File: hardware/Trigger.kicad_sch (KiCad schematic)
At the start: 2 parts, among them U6 MCP47FEB02A0T-E/ST, U7 Opamp_Dual

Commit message: Trig
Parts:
- added C30: 100n, symbol Device:C
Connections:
- net GND: now reaches U7.4 (V-)
- net GND: now also U6.5 (VSS), U6.6 (LAT/HVC), C30.1
- net VSYS: now reaches U7.8 (V+)
- net VSYS: now also U6.1 (VDD)
- net TRIG: now reaches U7.1
- net TRIG: now also U7.7
- net at U7.2 (-): now also U6.4 (VOUT1)
- net ASIG: now reaches U7.3 (+)
- net VREF: now reaches U6.2 (VREF)
- net VREF: now also C30.2
- net at U6.3 (VOUT0): now also U7.6 (-)
- net SDA: now reaches U6.7 (SCL)
- net SCL: now reaches U6.8 (SDA)
- net ASIG2: now reaches U7.5 (+)
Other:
- note added: "Possible resistor at TRIG output?"
- moved on the sheet: U6, U7C

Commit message: Trig finished
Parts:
- added C28: C, symbol Device:C
- added R14, R15: 0, symbol Device:R
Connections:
- net ASIG: now also R14.1; no longer U7.3 (+)
- net ASIG2: now also R15.2; no longer U7.5 (+)
- net GND: now also C28.2
- net TRIG: no longer U7.7
- net VSYS: now also C28.1
- new net: R15.1, U7.5 (+)
- new net: R14.2, U7.3 (+)
- new net TRIG2: U7.7

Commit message: updated trig
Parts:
- removed R14, R15: 0, symbol Device:R
- C28: value C -> 100n
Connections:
- net ASIG: now also U7.3 (+)
- net ASIG2: now also U7.5 (+)
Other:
- note removed: "Possible resistor at TRIG output?"
- moved on the sheet: C28, U7C
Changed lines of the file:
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@@
 	(generator_version "9.0")
 	(paper "A4")
-	(text "Possible resistor at TRIG output?\n"
-		(exclude_from_sim no)
-		(at 182.626 53.848 0)
-		(effects
-			(font
-				(size 1.27 1.27)
-			)
-		)
-	)
 	(junction
-		(at 184.15 69.85)
+		(at 187.96 74.93)
 		(diameter 0)
 		(color 0 0 0 0)
@@
 	(wire
 		(pts
-			(xy 143.51 62.23) (xy 151.13 62.23)
-		)
-		(stroke
-			(width 0)
-			(type default)
-		)
-	)
-	(wire
-		(pts
 			(xy 134.62 104.14) (xy 134.62 88.9)
 		)
@@
 	(wire
 		(pts
-			(xy 184.15 66.04) (xy 184.15 69.85)
+			(xy 191.77 74.93) (xy 187.96 74.93)
 		)
 		(stroke
@@
 	(wire
 		(pts
-			(xy 184.15 86.36) (xy 184.15 87.63)
+			(xy 171.45 74.93) (xy 170.18 74.93)
 		)
 		(stroke
@@
 	(wire
 		(pts
-			(xy 143.51 44.45) (xy 151.13 44.45)
-		)
-		(stroke
-			(width 0)
-			(type default)
-		)
-	)
-	(wire
-		(pts
 			(xy 190.5 110.49) (xy 190.5 114.3)
 		)
@@
 	(wire
 		(pts
-			(xy 195.58 69.85) (xy 199.39 69.85)
-		)
-		(stroke
-			(width 0)
-			(type default)
-		)
-	)
-	(wire
-		(pts
-			(xy 125.73 44.45) (xy 135.89 44.45)
+			(xy 187.96 86.36) (xy 187.96 90.17)
+		)
+		(stroke
+			(width 0)
+			(type default)
+		)
+	)
+	(wire
+		(pts
+			(xy 125.73 44.45) (xy 151.13 44.45)
 		)
 		(stroke
@@
 	(wire
 		(pts
-			(xy 184.15 69.85) (xy 187.96 69.85)
+			(xy 187.96 74.93) (xy 187.96 78.74)
 		)
 		(stroke
@@
 	(wire
 		(pts
-			(xy 125.73 62.23) (xy 135.89 62.23)
-		)
-		(stroke
-			(width 0)
-			(type default)
-		)
-	)
-	(wire
-		(pts
-			(xy 184.15 69.85) (xy 184.15 71.12)
+			(xy 125.73 62.23) (xy 151.13 62.23)
+		)
+		(stroke
+			(width 0)
+			(type default)
+		)
+	)
+	(wire
+		(pts
+			(xy 187.96 74.93) (xy 186.69 74.93)
 		)
 		(stroke
@@
 	(hierarchical_label "VSYS"
 		(shape input)
-		(at 184.15 66.04 90)
+		(at 191.77 74.93 0)
 		(effects
 			(font
@@
 	(symbol
 		(lib_id "Device:Opamp_Dual")
-		(at 186.69 78.74 0)
+		(at 179.07 77.47 270)
 		(unit 3)
 		(exclude_from_sim no)
@@
 		(fields_autoplaced yes)
 		(property "Reference" "U7"
-			(at 185.42 77.4699 0)
+			(at 180.3401 76.2 0)
 			(effects
 				(font
@@
 		)
 		(property "Value" "Opamp_Dual"
-			(at 185.42 80.0099 0)
+			(at 177.8001 76.2 0)
 			(effects
 				(font
@@
 		)
 		(property "Footprint" "Package_DIP:DIP-8_W7.62mm_Socket_LongPads"
-			(at 186.69 78.74 0)
+			(at 179.07 77.47 0)
 			(effects
 				(font
@@
 		)
 		(property "Datasheet" "~"
-			(at 186.69 78.74 0)
+			(at 179.07 77.47 0)
 			(effects
 				(font
@@
 		)
 		(property "Description" "Dual operational amplifier"
-			(at 186.69 78.74 0)
+			(at 179.07 77.47 0)
 			(effects
 				(font
@@
 		)
 		(property "Sim.Library" "${KICAD9_SYMBOL_DIR}/Simulation_SPICE.sp"
-			(at 186.69 78.74 0)
+			(at 179.07 77.47 0)
 			(effects
 				(font
@@
 		)
 		(property "Sim.Name" "kicad_builtin_opamp_dual"
-			(at 186.69 78.74 0)
+			(at 179.07 77.47 0)
 			(effects
 				(font
@@
 		)
 		(property "Sim.Device" "SUBCKT"
-			(at 186.69 78.74 0)
+			(at 179.07 77.47 0)
 			(effects
 				(font
@@
 		)
 		(property "Sim.Pins" "1=out1 2=in1- 3=in1+ 4=vee 5=in2+ 6=in2- 7=out2 8=vcc"
-			(at 186.69 78.74 0)
+			(at 179.07 77.47 0)
 			(effects
 				(font
@@
 	)
 	(symbol
-		(lib_id "Device:R")
-		(at 139.7 62.23 270)
-		(unit 1)
-		(exclude_from_sim no)
-		(in_bom yes)
-		(on_board yes)
-		(dnp no)
-		(fields_autoplaced yes)
-		(property "Reference" "R15"
-			(at 139.7 55.88 90)
-			(effects
-				(font
-					(size 1.27 1.27)
-				)
-			)
-		)
-		(property "Value" "0"
-			(at 139.7 58.42 90)
-			(effects
-				(font
-					(size 1.27 1.27)
-				)
-			)
-		)
-		(property "Footprint" ""
-			(at 139.7 60.452 90)
-			(effects
-				(font
-					(size 1.27 1.27)
-				)
-				(hide yes)
-			)
-		)
-		(property "Datasheet" "~"
-			(at 139.7 62.23 0)
-			(effects
-				(font
-					(size 1.27 1.27)
-				)
-				(hide yes)
-			)
-		)
-		(property "Description" "Resistor"
-			(at 139.7 62.23 0)
-			(effects
-				(font
-					(size 1.27 1.27)
-				)
-				(hide yes)
-			)
-		)
-		(pin "2"
-		)
-		(pin "1"
-		)
-		(instances
-			(project ""
-				(path "/94683f5c-9cd9-448e-be96-9792537b5cb8/865345ee-93ca-410b-9293-676d9f6f2ef0"
-					(reference "R15")
-					(unit 1)
-				)
-			)
-		)
-	)
-	(symbol
 		(lib_id "Device:Opamp_Dual")
 		(at 158.75 46.99 0)
@@
 	(symbol
 		(lib_id "Device:C")
-		(at 191.77 69.85 90)
+		(at 187.96 82.55 0)
 		(unit 1)
 		(exclude_from_sim no)
@@
 		(fields_autoplaced yes)
 		(property "Reference" "C28"
-			(at 191.77 62.23 90)
-			(effects
-				(font
-					(size 1.27 1.27)
-				)
-			)
-		)
-		(property "Value" "C"
-			(at 191.77 64.77 90)
+			(at 195.58 82.55 90)
+			(effects
+				(font
+					(size 1.27 1.27)
+				)
+			)
+		)
+		(property "Value" "100n"
+			(at 193.04 82.55 90)
 			(effects
 				(font
@@
 		)
 		(property "Footprint" ""
-			(at 195.58 68.8848 0)
+			(at 188.9252 86.36 0)
 			(effects
 				(font
@@
 		)
 		(property "Datasheet" "~"
-			(at 191.77 69.85 0)
+			(at 187.96 82.55 0)
 			(effects
 				(font
@@
 		)
 		(property "Description" "Unpolarized capacitor"
-			(at 191.77 69.85 0)
+			(at 187.96 82.55 0)
 			(effects
 				(font
@@
 	(symbol
 		(lib_id "power:GND")
-		(at 184.15 87.63 0)
+		(at 170.18 74.93 270)
 		(unit 1)
 		(exclude_from_sim no)
@@
 		(fields_autoplaced yes)
 		(property "Reference" "#PWR030"
-			(at 184.15 93.98 0)
+			(at 163.83 74.93 0)
 			(effects
 				(font
@@
 		)
 		(property "Value" "GND"
-			(at 184.15 92.71 0)
+			(at 165.1 74.93 0)
 			(effects
 				(font
@@
 		)
 		(property "Footprint" ""
-			(at 184.15 87.63 0)
+			(at 170.18 74.93 0)
 			(effects
 				(font
@@
 		)
 		(property "Datasheet" ""
-			(at 184.15 87.63 0)
+			(at 170.18 74.93 0)
 			(effects
 				(font
@@
 		)
 		(property "Description" "Power symbol creates a global label with name \"GND\" , ground"
-			(at 184.15 87.63 0)
+			(at 170.18 74.93 0)
 			(effects
 				(font
@@
 				(path "/94683f5c-9cd9-448e-be96-9792537b5cb8/865345ee-93ca-410b-9293-676d9f6f2ef0"
 					(reference "#PWR030")
-					(unit 1)
-				)
-			)
-		)
-	)
-	(symbol
-		(lib_id "Device:R")
-		(at 139.7 44.45 90)
-		(unit 1)
-		(exclude_from_sim no)
-		(in_bom yes)
-		(on_board yes)
-		(dnp no)
-		(fields_autoplaced yes)
-		(property "Reference" "R14"
-			(at 139.7 38.1 90)
-			(effects
-				(font
-					(size 1.27 1.27)
-				)
-			)
-		)
-		(property "Value" "0"
-			(at 139.7 40.64 90)
-			(effects
-				(font
-					(size 1.27 1.27)
-				)
-			)
-		)
-		(property "Footprint" ""
-			(at 139.7 46.228 90)
-			(effects
-				(font
-					(size 1.27 1.27)
-				)
-				(hide yes)
-			)
-		)
-		(property "Datasheet" "~"
-			(at 139.7 44.45 0)
-			(effects
-				(font
-					(size 1.27 1.27)
-				)
-				(hide yes)
-			)
-		)
-		(property "Description" "Resistor"
-			(at 139.7 44.45 0)
-			(effects
-				(font
-					(size 1.27 1.27)
-				)
-				(hide yes)
-			)
-		)
-		(pin "2"
-		)
-		(pin "1"
-		)
-		(instances
-			(project ""
-				(path "/94683f5c-9cd9-448e-be96-9792537b5cb8/865345ee-93ca-410b-9293-676d9f6f2ef0"
-					(reference "R14")
 					(unit 1)
 				)
@@
 	(symbol
 		(lib_id "power:GND")
-		(at 199.39 69.85 90)
+		(at 187.96 90.17 0)
 		(unit 1)
 		(exclude_from_sim no)
@@
 		(fields_autoplaced yes)
 		(property "Reference" "#PWR039"
-			(at 205.74 69.85 0)
+			(at 187.96 96.52 0)
 			(effects
 				(font
@@
 		)
 		(property "Value" "GND"
-			(at 203.2 69.8499 90)
+			(at 187.9601 93.98 90)
 			(effects
 				(font
@@
 		)
 		(property "Footprint" ""
-			(at 199.39 69.85 0)
+			(at 187.96 90.17 0)
 			(effects
 				(font
@@
 		)
 		(property "Datasheet" ""
-			(at 199.39 69.85 0)
+			(at 187.96 90.17 0)
 			(effects
 				(font
@@
 		)
 		(property "Description" "Power symbol creates a global label with name \"GND\" , ground"
-			(at 199.39 69.85 0)
-			(effects
-				(font
+			(at 187.96 90.17 0)
+			(effects
+				(font

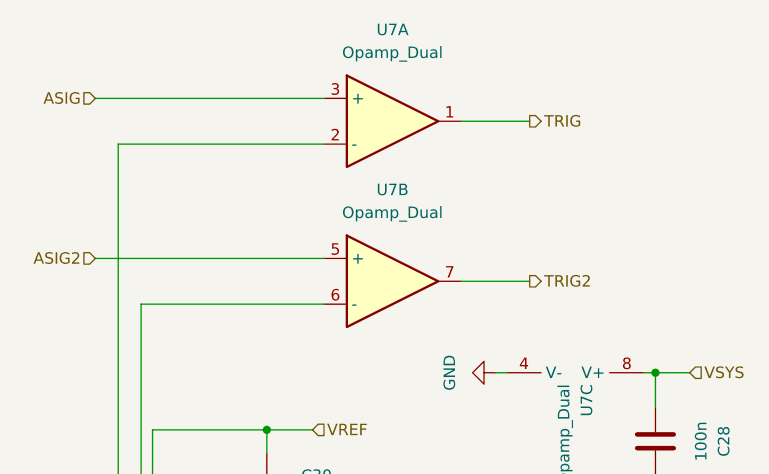
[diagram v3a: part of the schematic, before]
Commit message: connected analog i/o on main schematic and updated PSU naming
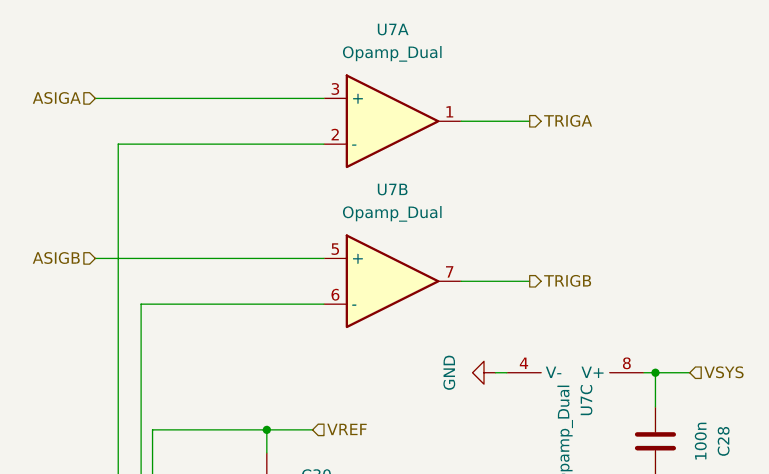
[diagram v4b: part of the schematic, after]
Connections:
- net ASIG renamed ASIGA
- net ASIG2 renamed ASIGB
- net TRIG renamed TRIGA
- net TRIG2 renamed TRIGB
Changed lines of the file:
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@@
 		)
 	)
-	(hierarchical_label "TRIG"
+	(hierarchical_label "TRIGA"
 		(shape output)
 		(at 173.99 46.99 0)
@@
 		)
 	)
-	(hierarchical_label "TRIG2"
+	(hierarchical_label "TRIGB"
 		(shape output)
 		(at 173.99 64.77 0)
@@
 		)
 	)
-	(hierarchical_label "ASIG"
+	(hierarchical_label "ASIGA"
 		(shape input)
 		(at 125.73 44.45 180)
@@
 		)
 	)
-	(hierarchical_label "ASIG2"
+	(hierarchical_label "ASIGB"
 		(shape input)
 		(at 125.73 62.23 180)

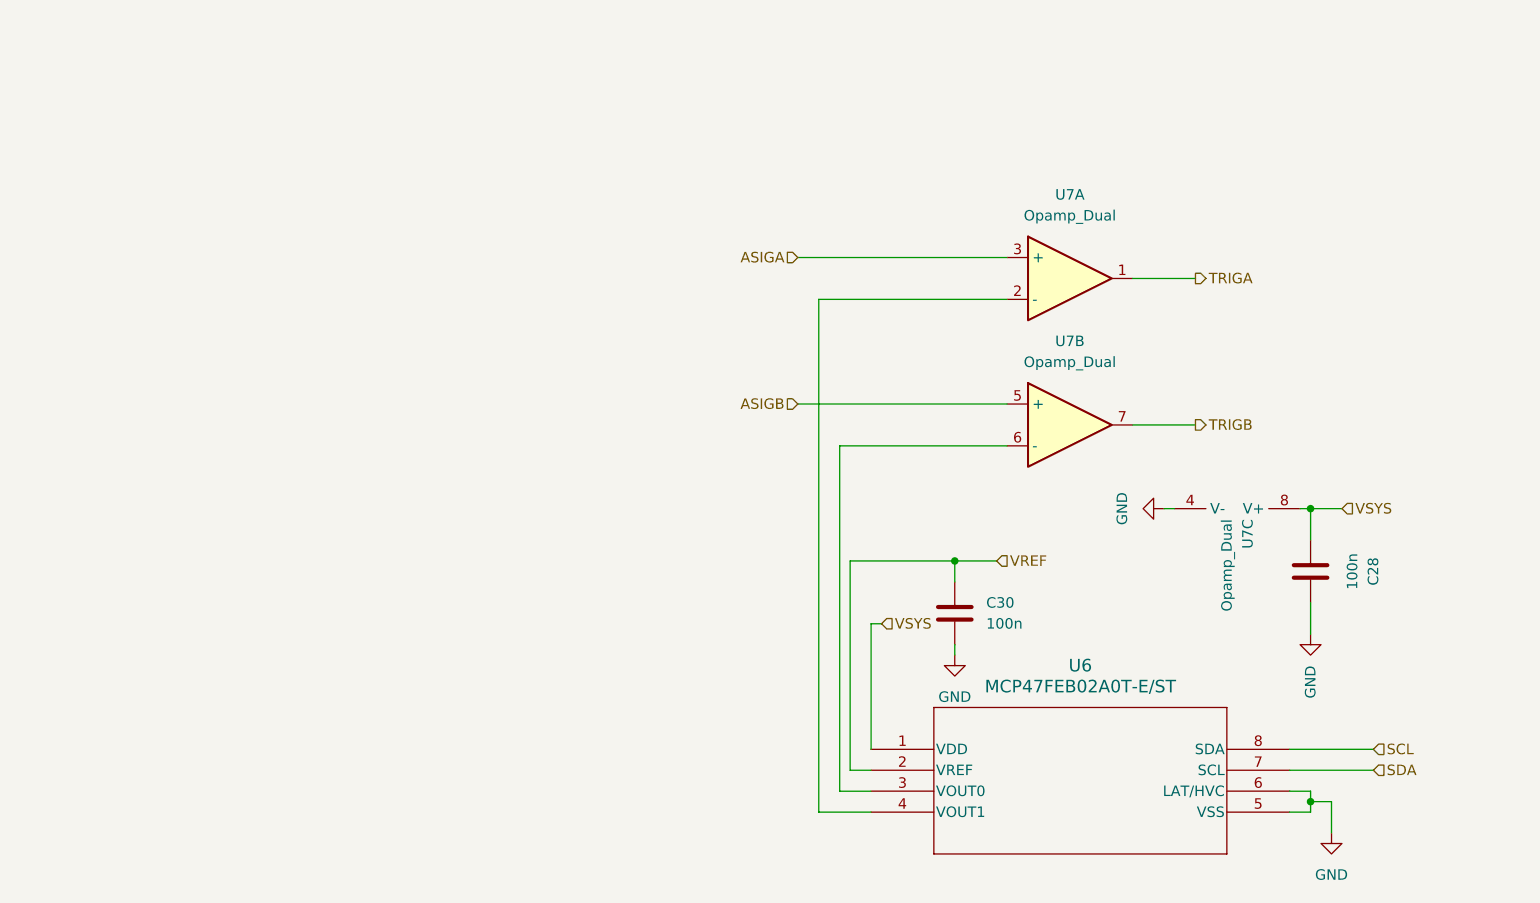
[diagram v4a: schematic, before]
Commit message: feat(hardware): Cleanup schematic, replace offset stage with non-inverting op amp, add neopixel LED
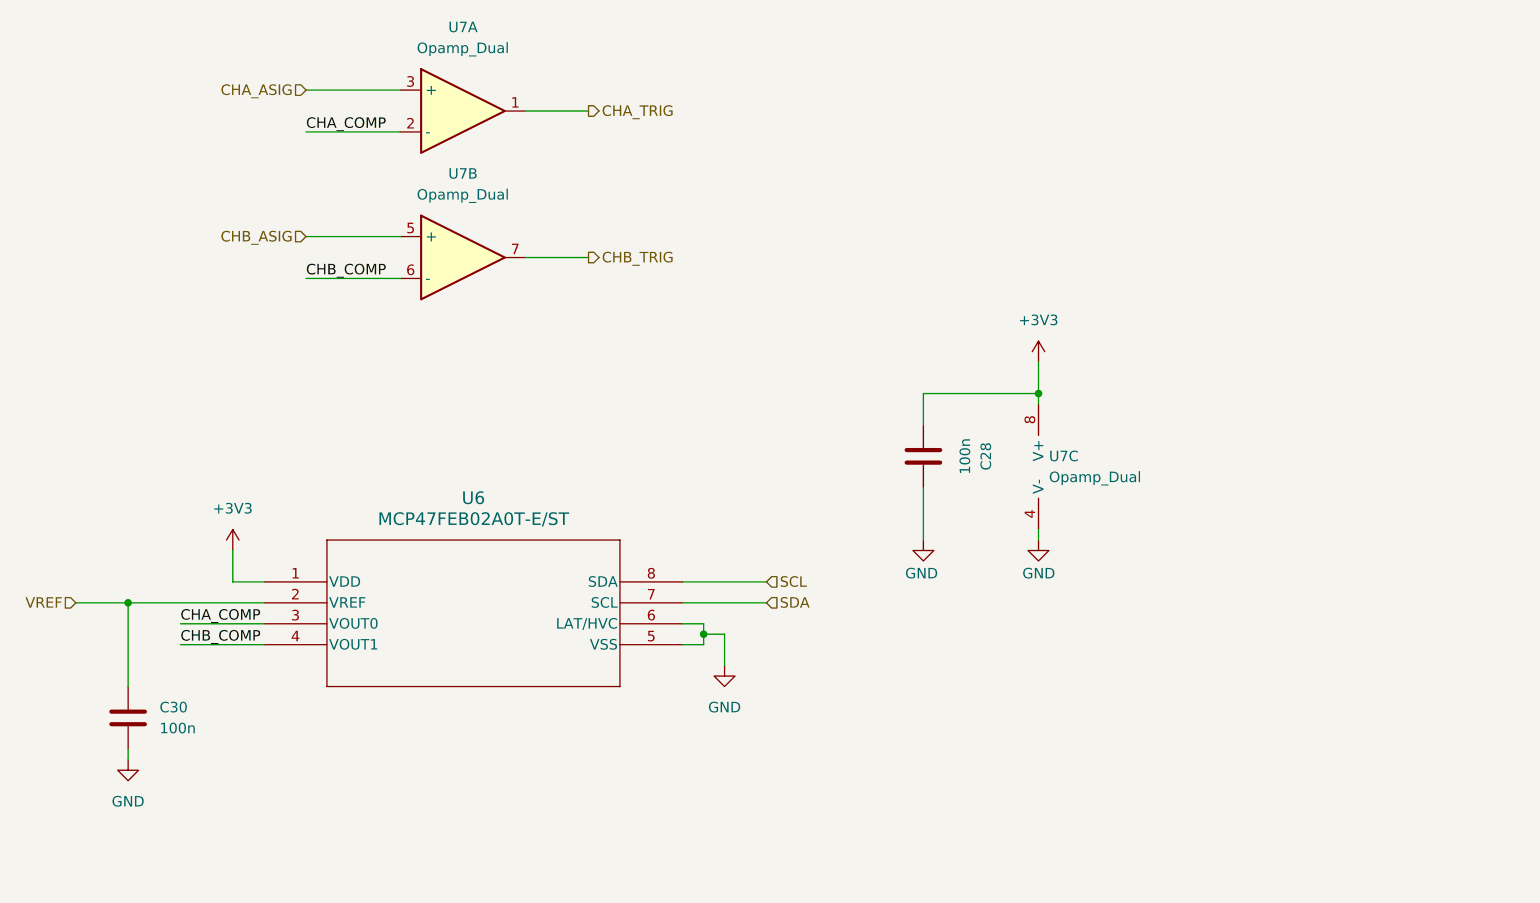
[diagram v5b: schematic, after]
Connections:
- net CHA_COMP: now reaches U7.2 (-)
- net CHA_COMP: now also U6.3 (VOUT0); no longer U6.4 (VOUT1)
- net CHB_COMP: now reaches U7.6 (-)
- net CHB_COMP: now also U6.4 (VOUT1); no longer U6.3 (VOUT0)
- net ASIGA renamed CHA_ASIG
- net ASIGB renamed CHB_ASIG
- net TRIGA renamed CHA_TRIG
- net TRIGB renamed CHB_TRIG
- net VSYS renamed +3V3
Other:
- moved on the sheet: C28, C30, U6, U7A, U7B, U7C
